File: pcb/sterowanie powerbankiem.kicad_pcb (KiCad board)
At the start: 2 copper layers, 54.4 x 26 mm, 26 parts, among them J1 USB_A, J2 Conn_01x01_Male, J3 Conn_01x01_Male, Q1 IRLML2060, SW1 SW_DIP_x01, U1 L78L33_SO8, U2 ATtiny13-20SSU

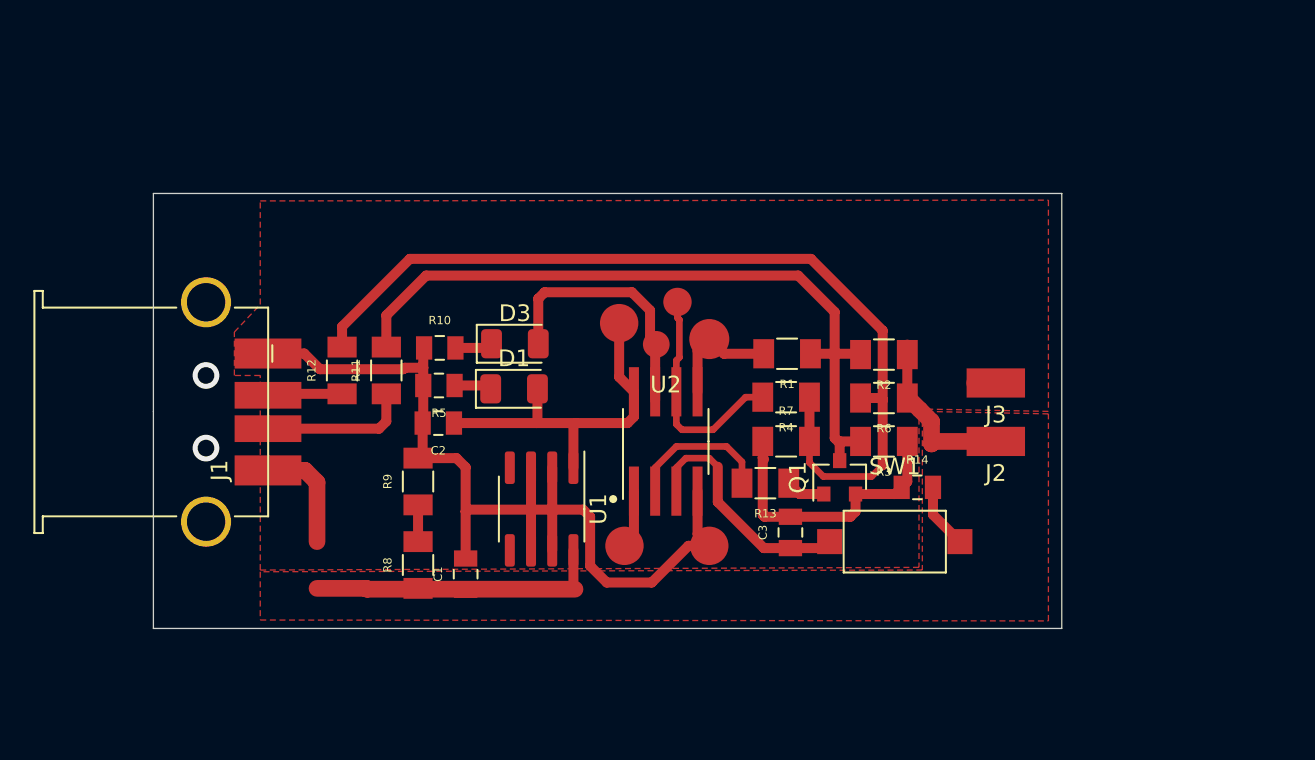
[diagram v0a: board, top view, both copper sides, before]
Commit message: PCB STM32G030J6 compatible
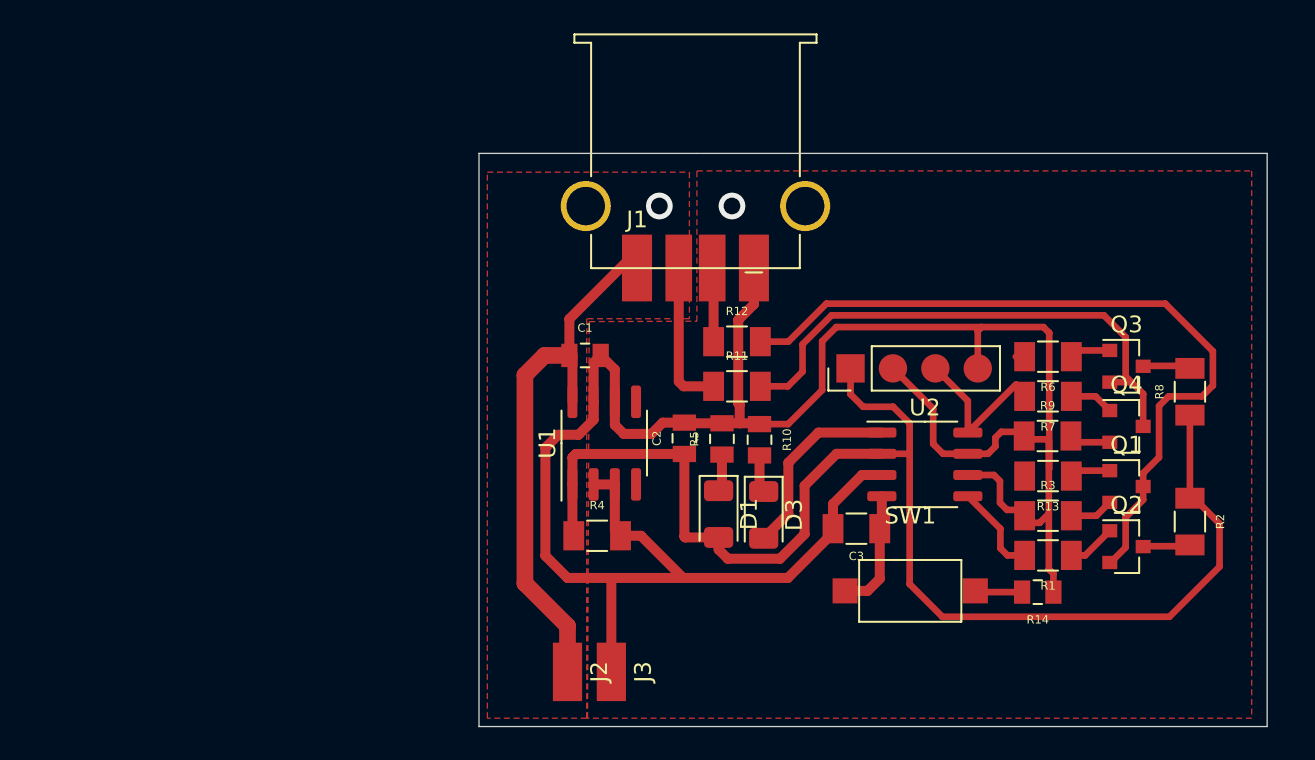
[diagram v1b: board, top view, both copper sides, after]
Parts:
- added J4: Conn_01x04, EKOLED-Złącza i przełączniki:PinHeader_1x04_P2.54mm, F.Cu at (77.2, 69.5)
- added Q2: IRLML2060, Package_TO_SOT_SMD:SOT-23, F.Cu at (93.7, 80.2)
- added Q3: IRLML2060, Package_TO_SOT_SMD:SOT-23, F.Cu at (93.7, 69.4)
- added Q4: IRLML2060, Package_TO_SOT_SMD:SOT-23, F.Cu at (93.7, 73.0)
- C3: footprint EKOLED-Elementy pasywne:C_0805 -> EKOLED-Elementy pasywne:C_1206
- R1: value 470R -> 1K
- R3: value 1K5 -> 2K
- R4: value 470R -> 100R
- R6: value 10K -> 1K
- R7: value 1K5 -> 1K
- R8: value 150R -> 10K
- R9: value 150R -> 2K
- U2: value ATtiny13-20SSU -> STM32G030J6; footprint EKOLED-Półprzewodniki:ATTiny13_SOIC-8 -> Package_SO:SO-8_3.9x4.9mm_P1.27mm
- moved R8 47.4 mm to (97.5, 70.9)
- moved R9 37.8 mm to (89.0, 73.6), turned to 0 degrees
- moved J1 35.5 mm to (67.9, 57.0), turned to 180 degrees
- moved J2 29.1 mm to (60.2, 87.7), turned to 180 degrees
- moved J3 28.8 mm to (62.9, 87.7), turned to 180 degrees
- moved R12 23.7 mm to (70.4, 67.9), turned to 0 degrees
- moved R11 21.0 mm to (70.4, 70.6), turned to 0 degrees
- moved R2 20.9 mm to (97.5, 78.7), turned to 270 degrees
- moved R10 19.9 mm to (71.8, 73.8), turned to 270 degrees
- moved R1 19.7 mm to (89.0, 80.7)
- moved D3 18.1 mm to (72.0, 78.3), turned to 270 degrees
- moved R5 17.2 mm to (69.5, 73.8), turned to 90 degrees
- moved Q1 17.2 mm to (93.7, 76.6), turned to 0 degrees
- moved R13 16.9 mm to (89.0, 76.0)
- moved R7 15.9 mm to (89.0, 71.2), turned to 180 degrees
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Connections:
- net PB0 renamed 5
- C3 pad 1: PB4 -> 4
- D3 pad 2: PB2 -> 1
- Q1 pad 2: GND -> Net-(Q1-Pad2)
- R1 pad 1: Net-(Q1-Pad3) -> Net-(Q2-Pad1)
- R11 pad 2: Net-(Q1-Pad3) -> Net-(Q3-Pad2)
- R12 pad 2: Net-(R12-Pad2) -> Net-(Q1-Pad3)
- R13 pad 2: PB3 -> 6
- R2 pad 1: +12V -> +3V3
- R2 pad 2: Net-(Q1-Pad3) -> Net-(Q2-Pad3)
- R3 pad 2: Net-(Q1-Pad3) -> Net-(Q1-Pad2)
- R4 pad 1: Net-(R12-Pad2) -> +3V3
- R4 pad 2: PB1 -> GND
- R6 pad 1: +12V -> Net-(Q3-Pad1)
- R6 pad 2: Net-(R12-Pad2) -> 8
- R7 pad 1: GND -> Net-(Q4-Pad1)
- R7 pad 2: Net-(R12-Pad2) -> 7
- R8 pad 1: +12V -> +3V3
- R8 pad 2: Net-(R8-Pad2) -> Net-(Q3-Pad3)
- R9 pad 1: Net-(R8-Pad2) -> GND
- R9 pad 2: GND -> Net-(Q4-Pad2)
- SW1 pad 1: PB4 -> 4
- U2 pad 1: Net-(U2-Pad1) -> 1
- U2 pad 2: PB3 -> +3V3
- U2 pad 3: PB4 -> GND
- U2 pad 4: GND -> 4
- U2 pad 6: PB1 -> 6
- U2 pad 7: PB2 -> 7
- U2 pad 8: +3V3 -> 8
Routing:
- net +3V3: track 21.7 -> 81.2 mm
- net Net-(R12-Pad2): track 55.4 -> 0.00 mm
- net GND: track 78.7 -> 124.3 mm
- net Net-(Q3-Pad2): track 0.00 -> 32.3 mm
- net PB2: track 16.1 -> 0.00 mm
- net PB4: track 14.2 -> 0.00 mm
- net PB1: track 13.6 -> 0.00 mm
- net 7: track 0.00 -> 12.1 mm
- net 1: track 0.00 -> 11.5 mm
- net 8: track 0.00 -> 9.27 mm
- net PB3: track 8.79 -> 0.00 mm
- net 4: track 0.00 -> 7.37 mm
- net 6: track 0.00 -> 5.05 mm
- net Net-(U2-Pad1): track 3.51 -> 0.00 mm
- net +12V: track 36.1 -> 32.8 mm
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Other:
- board size 54.4 x 26 mm -> 47.2 x 34.3 mm

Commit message: Drabinka rezystorowa (DAC) zamiast sterowania MOSFETami
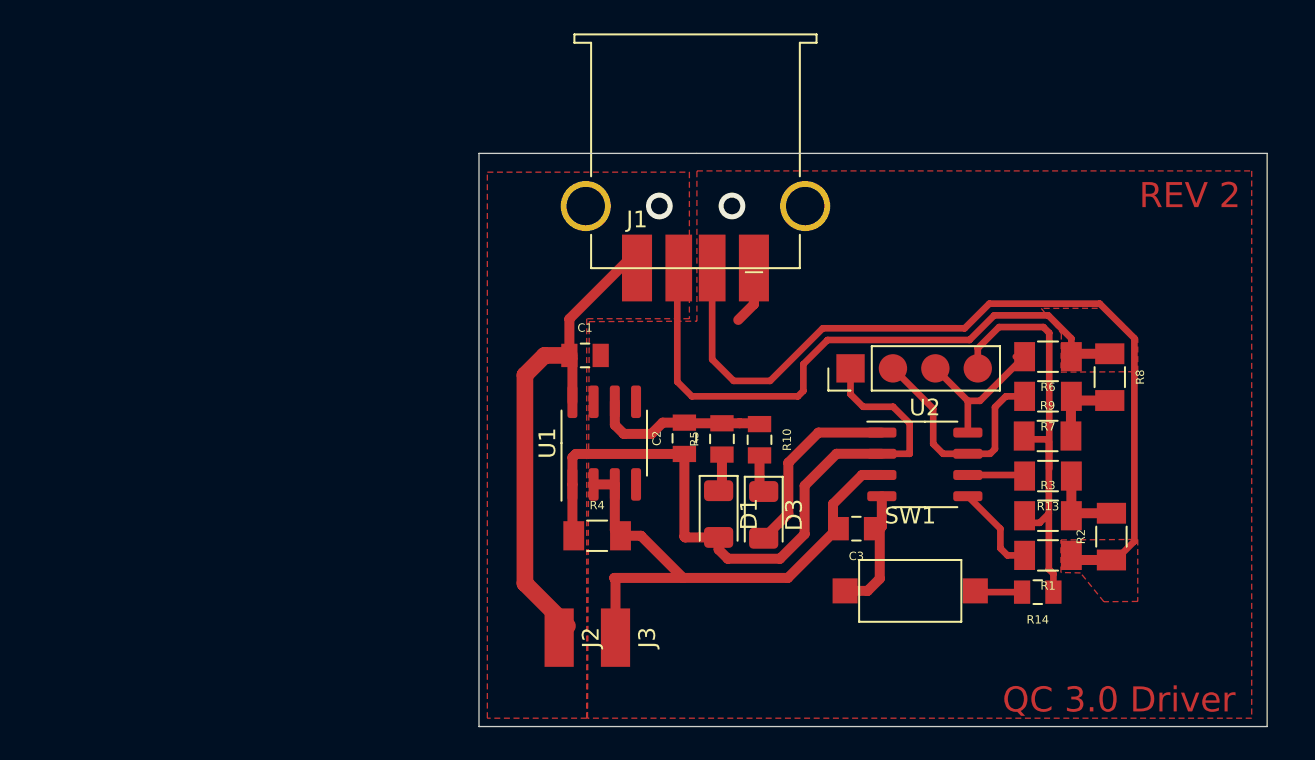
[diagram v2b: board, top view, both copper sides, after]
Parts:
- removed Q1, Q2, Q3, Q4: IRLML2060, Package_TO_SOT_SMD:SOT-23
- removed R11, R12: 0R, EKOLED-Elementy pasywne:R_1206
- C3: footprint EKOLED-Elementy pasywne:C_1206 -> EKOLED-Elementy pasywne:C_0805
- J2: value Conn_01x01_Male -> PAD_12V
- J3: value Conn_01x01_Male -> PAD_GND
- R13, R7: value 1K -> 100K
- R2, R8: value 10K -> 100K
- R3, R9: value 2K -> 22K
- moved R8 4.88 mm to (92.7, 70.0), turned to 270 degrees
- moved R2 4.79 mm to (92.8, 79.6), turned to 90 degrees
- moved J2 2.11 mm to (59.8, 85.7)
- moved J3 2.07 mm to (63.1, 85.7)
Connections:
- R1 pad 1: Net-(Q2-Pad1) -> D+
- R13 pad 1: Net-(Q1-Pad1) -> Net-(R13-Pad1)
- R2 pad 1: +3V3 -> D+
- R2 pad 2: Net-(Q2-Pad3) -> Net-(R13-Pad1)
- R3 pad 2: Net-(Q1-Pad2) -> Net-(R13-Pad1)
- R6 pad 1: Net-(Q3-Pad1) -> D-
- R7 pad 1: Net-(Q4-Pad1) -> Net-(R7-Pad1)
- R8 pad 1: +3V3 -> D-
- R8 pad 2: Net-(Q3-Pad3) -> Net-(R7-Pad1)
- R9 pad 2: Net-(Q4-Pad2) -> Net-(R7-Pad1)
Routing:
- net GND: track 124.3 -> 76.0 mm
- net D+: track 5.47 -> 51.6 mm
- net Net-(Q1-Pad3): track 45.6 -> 0.00 mm
- net +3V3: track 81.2 -> 42.9 mm
- net Net-(Q3-Pad2): track 32.3 -> 0.00 mm
- net D-: track 10.0 -> 38.8 mm
- net Net-(R13-Pad1): track 0.00 -> 4.84 mm
- net Net-(R7-Pad1): track 0.00 -> 4.79 mm
- net Net-(Q2-Pad1): track 2.91 -> 0.00 mm
- net +12V: track 32.8 -> 30.0 mm
- net Net-(Q4-Pad1): track 2.65 -> 0.00 mm
- net Net-(Q1-Pad2): track 2.63 -> 0.00 mm
- net Net-(Q4-Pad2): track 2.48 -> 0.00 mm
- net Net-(Q3-Pad1): track 2.46 -> 0.00 mm
- net Net-(Q1-Pad1): track 2.43 -> 0.00 mm
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- added copper zone on F.Cu, net D+
- added copper zone on F.Cu, net D-
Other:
- board text added: "QC 3.0 Driver"
- board text added: "REV 2"

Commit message: Tested with PCB
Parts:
- added REF**: EKOLED-LOGO, EKO-grafika:EKOLED-LOGO, F.Cu at (74.7, 88.0)
- J2, J3: footprint EKOLED-Pady:SMDPAD_1,75x3,5 -> EKOLED-Pady:SMDPAD_2,54x5,08
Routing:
- net GND: track 76.0 -> 74.7 mm

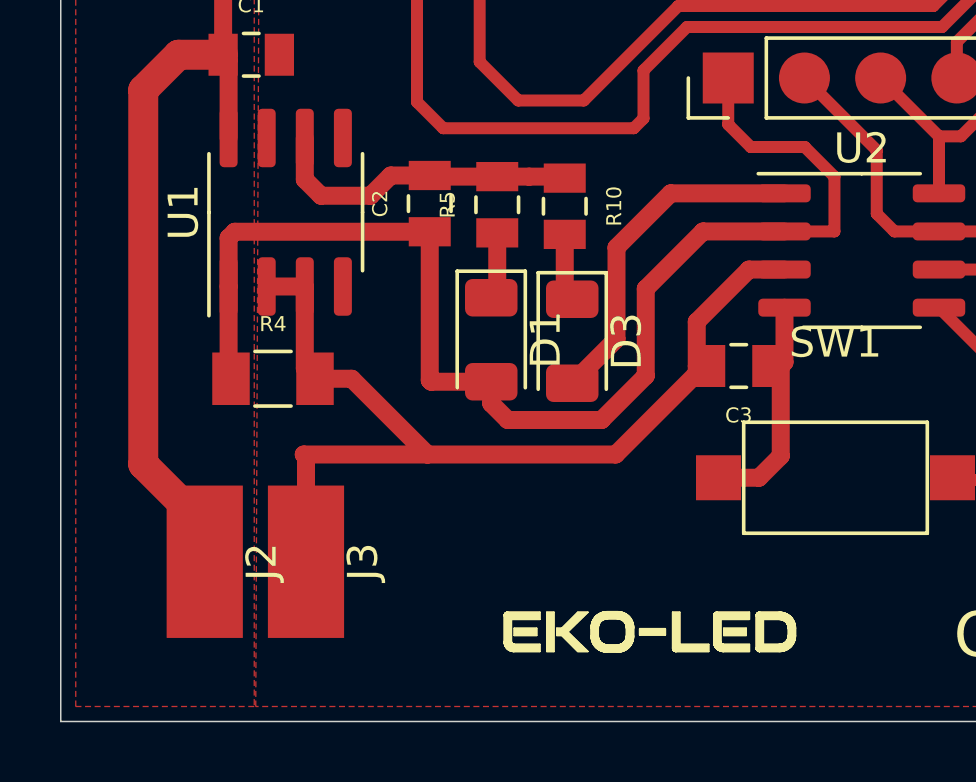
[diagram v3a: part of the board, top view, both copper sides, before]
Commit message: Resistors values better adjusted
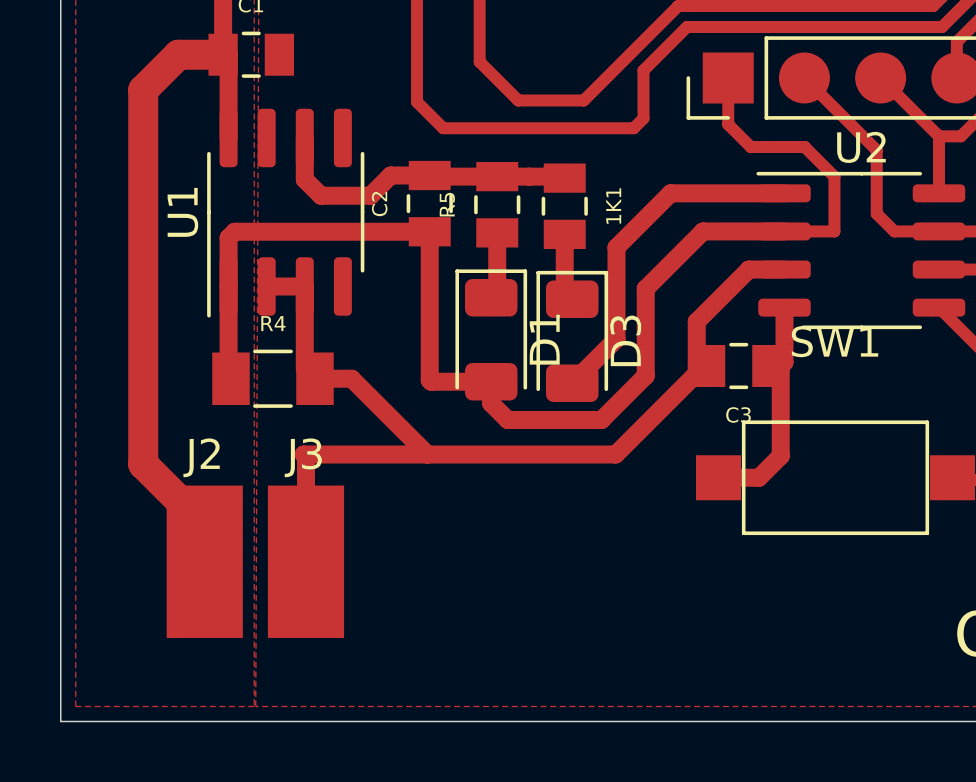
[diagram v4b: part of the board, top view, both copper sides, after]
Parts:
- removed REF**: EKOLED-LOGO, EKO-grafika:EKOLED-LOGO
- C3: value C -> 1uF
- R13, R7: value 100K -> 4.7K
- R14: value R -> 470R
- R2, R8: value 100K -> 2.7K
- R3, R9: value 22K -> 2.7K
- R4: value 100R -> 150R
- R5: value 50R -> 1K
- renumbered R10 to 1K1
